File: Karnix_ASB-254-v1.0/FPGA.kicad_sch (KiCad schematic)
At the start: 48 parts, among them U5 LFE5U-25F-BG256C, U7 W25Q128JVPIQ, Y2 25 MHz

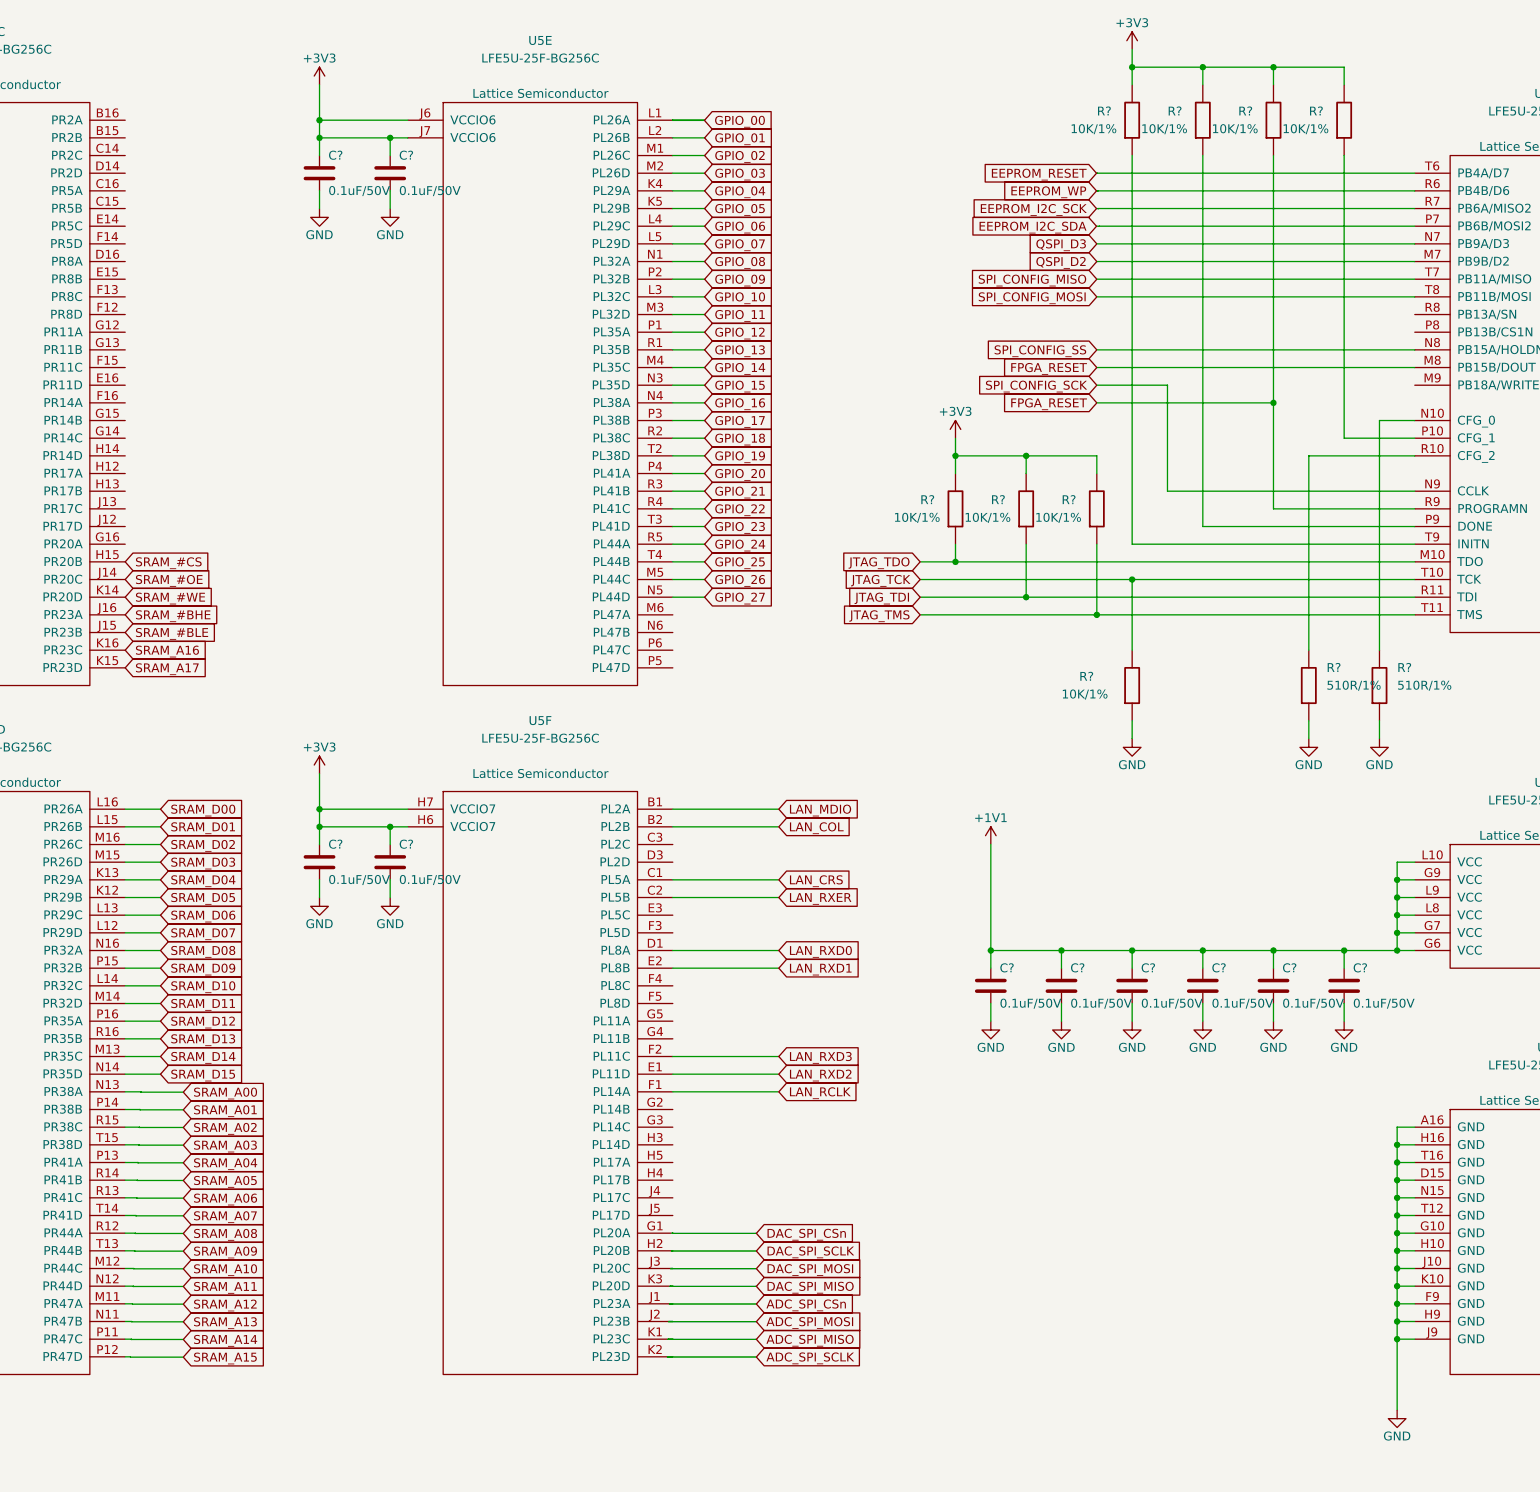
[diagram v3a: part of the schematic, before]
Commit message: Rewire DAC and ADC to ease routing
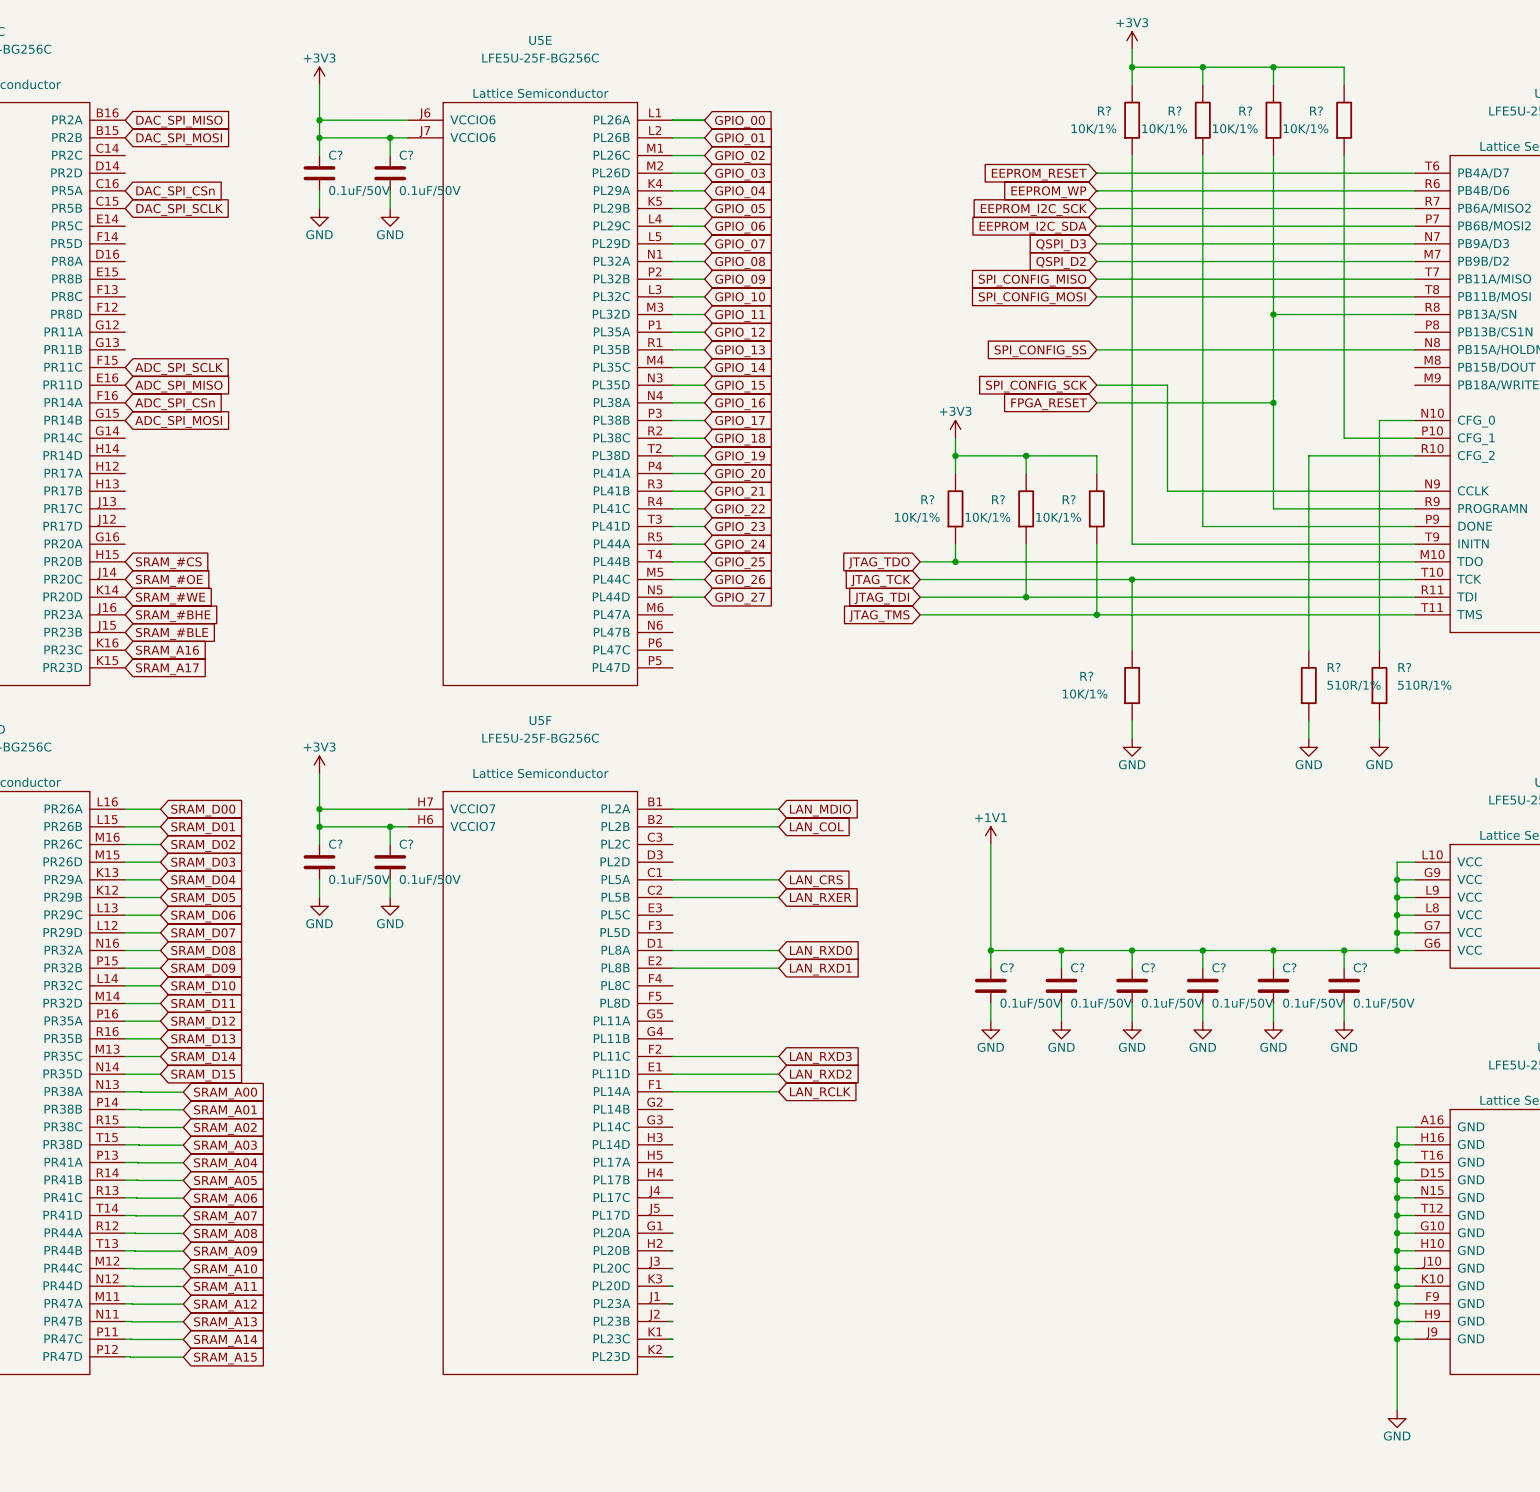
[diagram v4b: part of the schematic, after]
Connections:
- net ADC_SPI_CSn: now also U5.F16 (PR14A); no longer U5.J1 (PL23A)
- net ADC_SPI_MISO: now also U5.E16 (PR11D); no longer U5.K1 (PL23C)
- net ADC_SPI_MOSI: now also U5.G15 (PR14B); no longer U5.J2 (PL23B)
- net ADC_SPI_SCLK: now also U5.F15 (PR11C); no longer U5.K2 (PL23D)
- net DAC_SPI_CSn: now also U5.C16 (PR5A); no longer U5.G1 (PL20A)
- net DAC_SPI_MISO: now also U5.B16 (PR2A); no longer U5.K3 (PL20D)
- net DAC_SPI_MOSI: now also U5.B15 (PR2B); no longer U5.J3 (PL20C)
- net DAC_SPI_SCLK: now also U5.C15 (PR5B); no longer U5.H2 (PL20B)
- net FPGA_RESET: now also U5.R8 (PB13A/SN); no longer U5.M8 (PB15B/DOUT)
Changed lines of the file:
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@@
   (junction (at 27.305 36.195) (diameter 0) (color 0 0 0 0)
   )
+  (junction (at 321.945 61.595) (diameter 0) (color 0 0 0 0)
+  )
   (junction (at 27.305 33.655) (diameter 0) (color 0 0 0 0)
   )
@@
     (stroke (width 0) (type default))
   )
+  (wire (pts (xy 321.945 61.595) (xy 321.945 74.295))
+    (stroke (width 0) (type default))
+  )
   (wire (pts (xy 339.725 186.055) (xy 339.725 188.595))
     (stroke (width 0) (type default))
@@
     (stroke (width 0) (type default))
   )
-  (wire (pts (xy 247.6 203.86) (xy 235.1 203.86))
-    (stroke (width 0) (type default))
-  )
   (wire (pts (xy 165.2 188.64) (xy 158.5 188.64))
     (stroke (width 0) (type default))
@@
     (stroke (width 0) (type default))
   )
-  (wire (pts (xy 247.6 196.24) (xy 235.4 196.24))
-    (stroke (width 0) (type default))
-  )
   (wire (pts (xy 339.725 180.975) (xy 339.725 183.515))
     (stroke (width 0) (type default))
@@
     (stroke (width 0) (type default))
   )
-  (wire (pts (xy 247.6 208.94) (xy 234.9 208.94))
-    (stroke (width 0) (type default))
-  )
   (wire (pts (xy 234.8 211.48) (xy 234.8 211.455))
     (stroke (width 0) (type default))
@@
     (stroke (width 0) (type default))
   )
+  (wire (pts (xy 342.265 61.595) (xy 321.945 61.595))
+    (stroke (width 0) (type default))
+  )
   (wire (pts (xy 240.157 59.055) (xy 235.585 59.055))
     (stroke (width 0) (type default))
@@
     (stroke (width 0) (type default))
   )
-  (wire (pts (xy 342.265 69.215) (xy 296.545 69.215))
-    (stroke (width 0) (type default))
-  )
   (wire (pts (xy 240.157 79.375) (xy 235.585 79.375))
     (stroke (width 0) (type default))
@@
     (stroke (width 0) (type default))
   )
-  (wire (pts (xy 247.6 201.32) (xy 235.2 201.32))
-    (stroke (width 0) (type default))
-  )
   (wire (pts (xy 159 175.895) (xy 156.845 175.895))
     (stroke (width 0) (type default))
@@
     (stroke (width 0) (type default))
   )
-  (wire (pts (xy 247.6 206.4) (xy 235 206.4))
-    (stroke (width 0) (type default))
-  )
   (wire (pts (xy 342.265 51.435) (xy 296.545 51.435))
     (stroke (width 0) (type default))
@@
     (stroke (width 0) (type default))
   )
-  (wire (pts (xy 247.6 193.7) (xy 235.5 193.7))
-    (stroke (width 0) (type default))
-  )
   (wire (pts (xy 158.5 188.595) (xy 156.845 188.595))
     (stroke (width 0) (type default))
@@
     (stroke (width 0) (type default))
   )
-  (wire (pts (xy 321.945 38.735) (xy 321.945 74.295))
+  (wire (pts (xy 321.945 38.735) (xy 321.945 61.595))
     (stroke (width 0) (type default))
   )
@@
     (stroke (width 0) (type default))
   )
-  (wire (pts (xy 247.6 211.48) (xy 234.8 211.48))
-    (stroke (width 0) (type default))
-  )
   (wire (pts (xy 342.265 142.875) (xy 339.725 142.875))
     (stroke (width 0) (type default))
@@
   )
   (wire (pts (xy 84.5 158.16) (xy 78.6 158.16))
-    (stroke (width 0) (type default))
-  )
-  (wire (pts (xy 247.6 198.78) (xy 235.3 198.78))
     (stroke (width 0) (type default))
   )
@@
     )
   )
-  (global_label "ADC_SPI_MISO" (shape input) (at 247.6 208.94 0) (fields_autoplaced)
-    (effects (font (size 1.27 1.27)) (justify left))
-    (property "Intersheetrefs" "${INTERSHEET_REFS}" (at 259.8132 208.94 0)
+  (global_label "ADC_SPI_MISO" (shape input) (at 156.845 71.755 0) (fields_autoplaced)
+    (effects (font (size 1.27 1.27)) (justify left))
+    (property "Intersheetrefs" "${INTERSHEET_REFS}" (at 169.0582 71.755 0)
       (effects (font (size 1.27 1.27)) (justify left) hide)
     )
@@
     )
   )
-  (global_label "ADC_SPI_SCLK" (shape input) (at 247.6 211.48 0) (fields_autoplaced)
-    (effects (font (size 1.27 1.27)) (justify left))
-    (property "Intersheetrefs" "${INTERSHEET_REFS}" (at 260.0577 211.48 0)
+  (global_label "ADC_SPI_SCLK" (shape input) (at 156.845 69.215 0) (fields_autoplaced)
+    (effects (font (size 1.27 1.27)) (justify left))
+    (property "Intersheetrefs" "${INTERSHEET_REFS}" (at 169.3027 69.215 0)
       (effects (font (size 1.27 1.27)) (justify left) hide)
     )
@@
     )
   )
-  (global_label "DAC_SPI_MOSI" (shape input) (at 247.6 198.78 0) (fields_autoplaced)
-    (effects (font (size 1.27 1.27)) (justify left))
-    (property "Intersheetrefs" "${INTERSHEET_REFS}" (at 259.8132 198.78 0)
+  (global_label "DAC_SPI_MOSI" (shape input) (at 156.845 36.195 0) (fields_autoplaced)
+    (effects (font (size 1.27 1.27)) (justify left))
+    (property "Intersheetrefs" "${INTERSHEET_REFS}" (at 169.0582 36.195 0)
       (effects (font (size 1.27 1.27)) (justify left) hide)
     )
@@
     )
   )
-  (global_label "FPGA_RESET" (shape input) (at 296.545 69.215 180)
-    (effects (font (size 1.27 1.27)) (justify right))
-    (property "Intersheetrefs" "${INTERSHEET_REFS}" (at 296.545 69.215 0)
-      (effects (font (size 1.27 1.27)) hide)
-    )
-  )
   (global_label "LED3" (shape input) (at 84.455 188.595 0)
     (effects (font (size 1.27 1.27)) (justify left))
@@
     )
   )
-  (global_label "ADC_SPI_MOSI" (shape input) (at 247.6 206.4 0) (fields_autoplaced)
-    (effects (font (size 1.27 1.27)) (justify left))
-    (property "Intersheetrefs" "${INTERSHEET_REFS}" (at 259.8132 206.4 0)
+  (global_label "ADC_SPI_MOSI" (shape input) (at 156.845 76.835 0) (fields_autoplaced)
+    (effects (font (size 1.27 1.27)) (justify left))
+    (property "Intersheetrefs" "${INTERSHEET_REFS}" (at 169.0582 76.835 0)
       (effects (font (size 1.27 1.27)) (justify left) hide)
     )
@@
     )
   )
-  (global_label "ADC_SPI_CSn" (shape input) (at 247.6 203.86 0) (fields_autoplaced)
-    (effects (font (size 1.27 1.27)) (justify left))
-    (property "Intersheetrefs" "${INTERSHEET_REFS}" (at 259.0837 203.86 0)
+  (global_label "ADC_SPI_CSn" (shape input) (at 156.845 74.295 0) (fields_autoplaced)
+    (effects (font (size 1.27 1.27)) (justify left))
+    (property "Intersheetrefs" "${INTERSHEET_REFS}" (at 168.3287 74.295 0)
       (effects (font (size 1.27 1.27)) (justify left) hide)
     )
@@
     )
   )
-  (global_label "DAC_SPI_MISO" (shape input) (at 247.6 201.32 0) (fields_autoplaced)
-    (effects (font (size 1.27 1.27)) (justify left))
-    (property "Intersheetrefs" "${INTERSHEET_REFS}" (at 259.8132 201.32 0)
+  (global_label "DAC_SPI_MISO" (shape input) (at 156.845 33.655 0) (fields_autoplaced)
+    (effects (font (size 1.27 1.27)) (justify left))
+    (property "Intersheetrefs" "${INTERSHEET_REFS}" (at 169.0582 33.655 0)
       (effects (font (size 1.27 1.27)) (justify left) hide)
     )
@@
     )
   )
-  (global_label "DAC_SPI_CSn" (shape input) (at 247.6 193.7 0) (fields_autoplaced)
-    (effects (font (size 1.27 1.27)) (justify left))
-    (property "Intersheetrefs" "${INTERSHEET_REFS}" (at 259.0837 193.7 0)
+  (global_label "DAC_SPI_CSn" (shape input) (at 156.845 43.815 0) (fields_autoplaced)
+    (effects (font (size 1.27 1.27)) (justify left))
+    (property "Intersheetrefs" "${INTERSHEET_REFS}" (at 168.3287 43.815 0)
       (effects (font (size 1.27 1.27)) (justify left) hide)
     )
@@
     )
   )
-  (global_label "DAC_SPI_SCLK" (shape input) (at 247.6 196.24 0) (fields_autoplaced)
-    (effects (font (size 1.27 1.27)) (justify left))
-    (property "Intersheetrefs" "${INTERSHEET_REFS}" (at 260.0577 196.24 0)
+  (global_label "DAC_SPI_SCLK" (shape input) (at 156.845 46.355 0) (fields_autoplaced)
+    (effects (font (size 1.27 1.27)) (justify left))
+    (property "Intersheetrefs" "${INTERSHEET_REFS}" (at 169.3027 46.355 0)
       (effects (font (size 1.27 1.27)) (justify left) hide)
     )

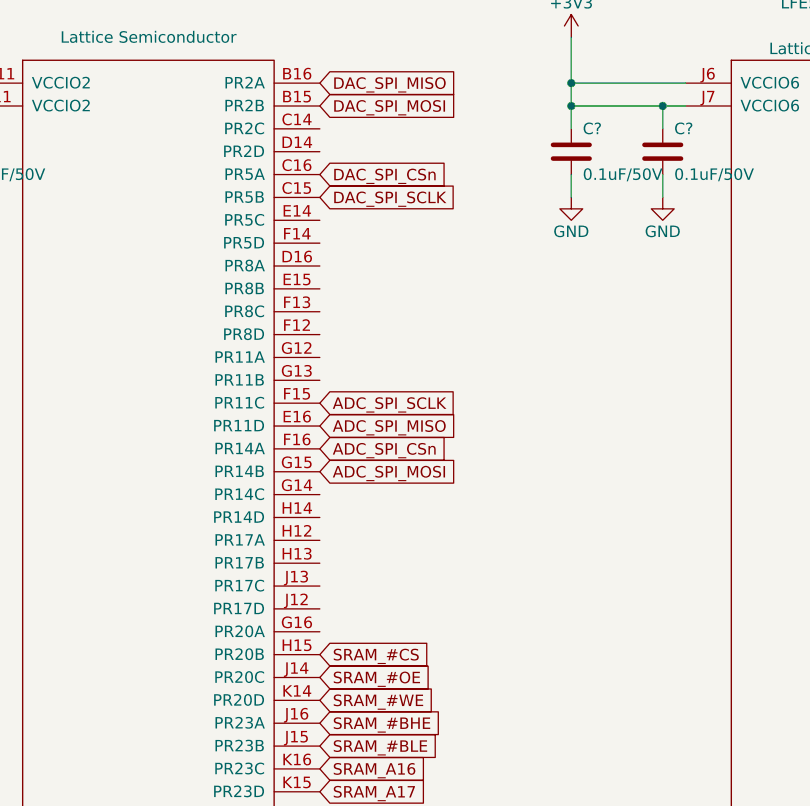
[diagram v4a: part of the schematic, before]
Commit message: Exchanges signals on DAC and ADC to ease routing
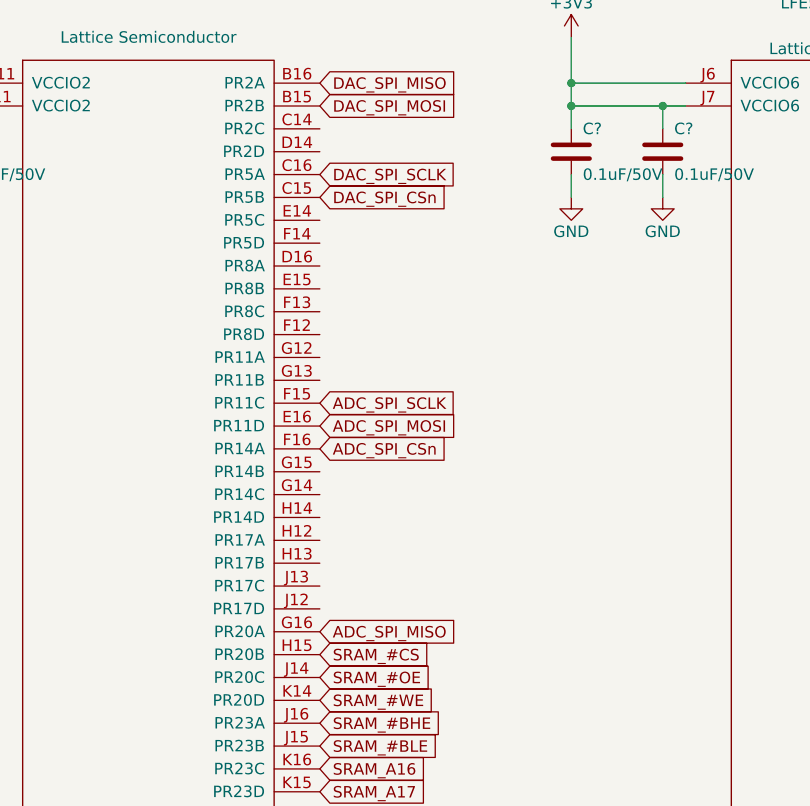
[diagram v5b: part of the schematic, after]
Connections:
- net ADC_SPI_MISO: now also U5.G16 (PR20A); no longer U5.E16 (PR11D)
- net ADC_SPI_MOSI: now also U5.E16 (PR11D); no longer U5.G15 (PR14B)
- net DAC_SPI_CSn: now also U5.C15 (PR5B); no longer U5.C16 (PR5A)
- net DAC_SPI_SCLK: now also U5.C16 (PR5A); no longer U5.C15 (PR5B)
